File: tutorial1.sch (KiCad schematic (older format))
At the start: 5 parts, among them IC1 PIC12C508A-I/SN, J1 MYCONN3

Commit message: busses
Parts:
- added P1, P2, P3, P?: USB_OTG, symbol USB_OTG
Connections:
- net labels added: a1, a2, a3, a4, a5, a[1...5], b1, b2, b3, b4, b5
- wire segments 18 -> 38
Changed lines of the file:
@@
 $EndComp
 $Comp
-L VCC #PWR01
+L VCC #PWR1
 U 1 1 59841EA6
 P 2450 1650
-F 0 "#PWR01" H 2450 1500 50  0001 C CNN
+F 0 "#PWR1" H 2450 1500 50  0001 C CNN
 F 1 "VCC" H 2450 1800 50  0000 C CNN
 F 2 "" H 2450 1650 50  0000 C CNN
@@
 $EndComp
 $Comp
-L VCC #PWR02
+L VCC #PWR7
 U 1 1 59841EF5
 P 5150 1300
-F 0 "#PWR02" H 5150 1150 50  0001 C CNN
+F 0 "#PWR7" H 5150 1150 50  0001 C CNN
 F 1 "VCC" H 5150 1450 50  0000 C CNN
 F 2 "" H 5150 1300 50  0000 C CNN
@@
 $EndComp
 $Comp
-L VCC #PWR03
+L VCC #PWR5
 U 1 1 59841F14
 P 3550 2800
-F 0 "#PWR03" H 3550 2650 50  0001 C CNN
+F 0 "#PWR5" H 3550 2650 50  0001 C CNN
 F 1 "VCC" H 3550 2950 50  0000 C CNN
 F 2 "" H 3550 2800 50  0000 C CNN
@@
 $EndComp
 $Comp
-L GND #PWR04
+L GND #PWR2
 U 1 1 59842025
 P 2450 2550
-F 0 "#PWR04" H 2450 2300 50  0001 C CNN
+F 0 "#PWR2" H 2450 2300 50  0001 C CNN
 F 1 "GND" H 2450 2400 50  0000 C CNN
 F 2 "" H 2450 2550 50  0000 C CNN
@@
 $EndComp
 $Comp
-L GND #PWR05
+L GND #PWR6
 U 1 1 59842043
 P 3550 3200
-F 0 "#PWR05" H 3550 2950 50  0001 C CNN
+F 0 "#PWR6" H 3550 2950 50  0001 C CNN
 F 1 "GND" H 3550 3050 50  0000 C CNN
 F 2 "" H 3550 3200 50  0000 C CNN
@@
 	1    0    0    -1
 $EndComp
-Wire Wire Line
-	4050 1850 4200 1850
-Wire Wire Line
-	4200 1850 4200 1350
-Wire Wire Line
-	4050 1950 4750 1950
-Wire Wire Line
-	2650 1850 2450 1850
-Wire Wire Line
-	2450 1850 2450 1650
-Wire Wire Line
-	2650 2450 2450 2450
-Wire Wire Line
-	2450 2450 2450 2550
-Wire Wire Line
-	3400 2900 3550 2900
-Wire Wire Line
-	3550 2900 3550 2800
-Wire Wire Line
-	3400 3100 3550 3100
-Wire Wire Line
-	3550 3100 3550 3200
-Wire Wire Line
-	3400 3000 3950 3000
-Wire Wire Line
-	4250 3000 4750 3000
-Wire Wire Line
-	4600 1350 4700 1350
-Wire Wire Line
-	5000 1350 5150 1350
-Wire Wire Line
-	5150 1350 5150 1300
 Text Label 4450 1950 0    60   ~ 0
 INPUT
@@
 NoConn ~ 2500 1250
 $Comp
-L PWR_FLAG #FLG06
+L PWR_FLAG #FLG1
 U 1 1 598423A3
 P 2800 1200
-F 0 "#FLG06" H 2800 1295 50  0001 C CNN
+F 0 "#FLG1" H 2800 1295 50  0001 C CNN
 F 1 "PWR_FLAG" H 2800 1380 50  0000 C CNN
 F 2 "" H 2800 1200 50  0000 C CNN
@@
 $EndComp
 $Comp
-L PWR_FLAG #FLG07
+L PWR_FLAG #FLG2
 U 1 1 598423C1
 P 3150 1050
-F 0 "#FLG07" H 3150 1145 50  0001 C CNN
+F 0 "#FLG2" H 3150 1145 50  0001 C CNN
 F 1 "PWR_FLAG" H 3150 1230 50  0000 C CNN
 F 2 "" H 3150 1050 50  0000 C CNN
@@
 $EndComp
 $Comp
-L VCC #PWR08
+L VCC #PWR3
 U 1 1 598423E4
 P 2800 1050
-F 0 "#PWR08" H 2800 900 50  0001 C CNN
+F 0 "#PWR3" H 2800 900 50  0001 C CNN
 F 1 "VCC" H 2800 1200 50  0000 C CNN
 F 2 "" H 2800 1050 50  0000 C CNN
@@
 $EndComp
 $Comp
-L GND #PWR09
+L GND #PWR4
 U 1 1 5984246D
 P 3150 1200
-F 0 "#PWR09" H 3150 950 50  0001 C CNN
+F 0 "#PWR4" H 3150 950 50  0001 C CNN
 F 1 "GND" H 3150 1050 50  0000 C CNN
 F 2 "" H 3150 1200 50  0000 C CNN
@@
 	1    0    0    -1
 $EndComp
+$Comp
+L USB_OTG P1
+U 1 1 59AE7FC8
+P 2950 4450
+F 0 "P1" H 3275 4325 50  0000 C CNN
+F 1 "USB_OTG" H 2950 4650 50  0000 C CNN
+F 2 "" V 2900 4350 50  0000 C CNN
+F 3 "" V 2900 4350 50  0000 C CNN
+	1    2950 4450
+	0    -1   1    0
+$EndComp
+$Comp
+L USB_OTG P2
+U 1 1 59AE8338
+P 2950 5400
+F 0 "P2" H 3275 5275 50  0000 C CNN
+F 1 "USB_OTG" H 2950 5600 50  0000 C CNN
+F 2 "" V 2900 5300 50  0000 C CNN
+F 3 "" V 2900 5300 50  0000 C CNN
+	1    2950 5400
+	0    -1   1    0
+$EndComp
+$Comp
+L USB_OTG P3
+U 1 1 59AE8397
+P 2950 6350
+F 0 "P3" H 3275 6225 50  0000 C CNN
+F 1 "USB_OTG" H 2950 6550 50  0000 C CNN
+F 2 "" V 2900 6250 50  0000 C CNN
+F 3 "" V 2900 6250 50  0000 C CNN
+	1    2950 6350
+	0    -1   1    0
+$EndComp
+Text Label 3250 4250 0    60   ~ 0
+a1
+Text Label 3250 4350 0    60   ~ 0
+a2
+Text Label 3250 4450 0    60   ~ 0
+a3
+Text Label 3250 4550 0    60   ~ 0
+a4
+Text Label 3250 4650 0    60   ~ 0
+a5
+Text Label 3250 5200 0    60   ~ 0
+a1
+Text Label 3250 5300 0    60   ~ 0
+a2
+Text Label 3250 5400 0    60   ~ 0
+a3
+Text Label 3250 5500 0    60   ~ 0
+a4
+Text Label 3250 5600 0    60   ~ 0
+a5
+Text Label 3250 6150 0    60   ~ 0
+a1
+Text Label 3250 6250 0    60   ~ 0
+a2
+Text Label 3250 6350 0    60   ~ 0
+a3
+Text Label 3250 6450 0    60   ~ 0
+a4
+Text Label 3250 6550 0    60   ~ 0
+a5
+Entry Wire Line
+	3650 4250 3750 4350
+Entry Wire Line
+	3650 4350 3750 4450
+Entry Wire Line
+	3650 4450 3750 4550
+Entry Wire Line
+	3650 4550 3750 4650
+Entry Wire Line
+	3650 4650 3750 4750
+Entry Wire Line
+	3650 5200 3750 5300
+Entry Wire Line
+	3650 5300 3750 5400
+Entry Wire Line
+	3650 5400 3750 5500
+Entry Wire Line
+	3650 5500 3750 5600
+Entry Wire Line
+	3650 5600 3750 5700
+Entry Wire Line
+	3650 6150 3750 6250
+Entry Wire Line
+	3650 6250 3750 6350
+Entry Wire Line
+	3650 6350 3750 6450
+Entry Wire Line
+	3650 6450 3750 6550
+Entry Wire Line
+	3650 6550 3750 6650
+Text Label 3750 5000 0    60   ~ 0
+a[1...5]
+$Comp
+L USB_OTG P?
+U 1 1 59AF0BD4
+P 5600 4450
+F 0 "P?" H 5925 4325 50  0000 C CNN
+F 1 "USB_OTG" H 5600 4650 50  0000 C CNN
+F 2 "" V 5550 4350 50  0000 C CNN
+F 3 "" V 5550 4350 50  0000 C CNN
+	1    5600 4450
+	0    1    1    0
+$EndComp
+Text Label 5150 4250 0    60   ~ 0
+b1
+Text Label 5150 4350 0    60   ~ 0
+b2
+Text Label 5150 4450 0    60   ~ 0
+b3
+Text Label 5150 4550 0    60   ~ 0
+b4
+Text Label 5150 4650 0    60   ~ 0
+b5
+Wire Wire Line
+	4050 1850 4200 1850
+Wire Wire Line
+	4200 1850 4200 1350
+Wire Wire Line
+	4050 1950 4750 1950
+Wire Wire Line
+	2650 1850 2450 1850
+Wire Wire Line
+	2450 1850 2450 1650
+Wire Wire Line
+	2650 2450 2450 2450
+Wire Wire Line
+	2450 2450 2450 2550
+Wire Wire Line
+	3400 2900 3550 2900
+Wire Wire Line
+	3550 2900 3550 2800
+Wire Wire Line
+	3400 3100 3550 3100
+Wire Wire Line
+	3550 3100 3550 3200
+Wire Wire Line
+	3400 3000 3950 3000
+Wire Wire Line
+	4250 3000 4750 3000
+Wire Wire Line
+	4600 1350 4700 1350
+Wire Wire Line
+	5000 1350 5150 1350
+Wire Wire Line
+	5150 1350 5150 1300
 Wire Wire Line
 	3150 1050 3150 1200
 Wire Wire Line
 	2800 1200 2800 1050
+Wire Bus Line
+	3750 4200 3750 6700
+Wire Wire Line
+	3250 4250 3650 4250
+Wire Wire Line
+	3250 4350 3650 4350
+Wire Wire Line
+	3250 4450 3650 4450
+Wire Wire Line
+	3250 4550 3650 4550
+Wire Wire Line
+	3250 4650 3650 4650
+Wire Wire Line
+	3250 5200 3650 5200
+Wire Wire Line
+	3250 5300 3650 5300
+Wire Wire Line
+	3250 5400 3650 5400
+Wire Wire Line
+	3250 5500 3650 5500
+Wire Wire Line
+	3250 5600 3650 5600
+Wire Wire Line
+	3250 6150 3650 6150
+Wire Wire Line
+	3250 6250 3650 6250
+Wire Wire Line
+	3250 6350 3650 6350
+Wire Wire Line
+	3250 6450 3650 6450
+Wire Wire Line
+	3250 6550 3650 6550
+Wire Bus Line
+	4850 4050 4850 5150
+Wire Wire Line
+	5300 4250 4950 4250
+Wire Wire Line
+	5300 4350 4950 4350
+Wire Wire Line
+	5300 4450 4950 4450
+Wire Wire Line
+	5300 4550 4950 4550
+Wire Wire Line
+	5300 4650 4950 4650
+Entry Wire Line
+	4850 4550 4950 4650
+Entry Wire Line
+	4850 4450 4950 4550
+Entry Wire Line
+	4850 4350 4950 4450
+Entry Wire Line
+	4850 4250 4950 4350
+Entry Wire Line
+	4850 4150 4950 4250
 $EndSCHEMATC

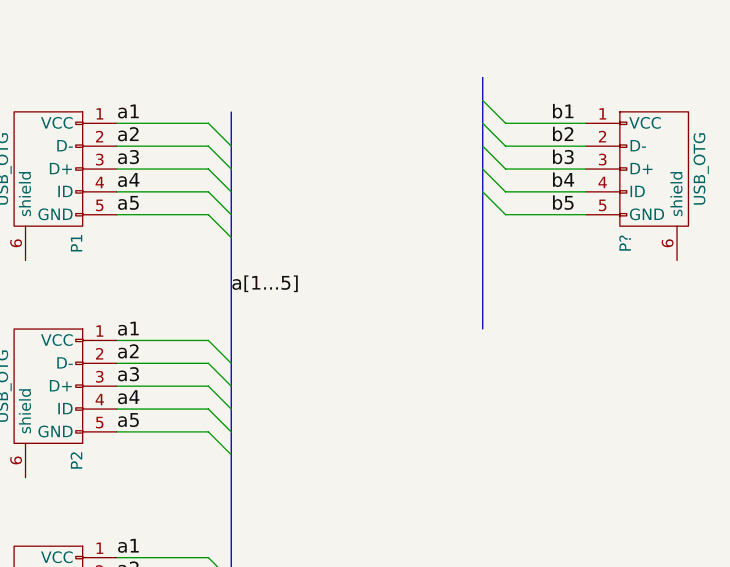
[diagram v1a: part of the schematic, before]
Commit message: bus labels
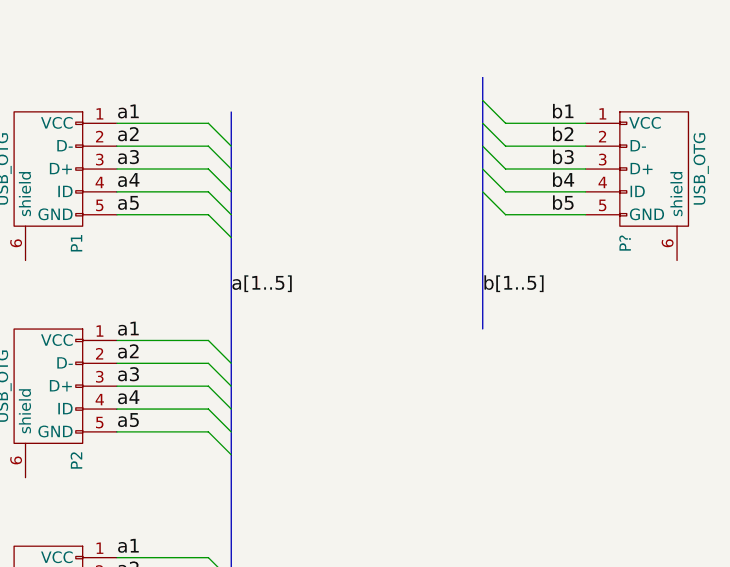
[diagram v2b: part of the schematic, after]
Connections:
- net labels added: a[1..5], b[1..5]
- net labels removed: a[1...5]
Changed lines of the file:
@@
 	3650 6550 3750 6650
 Text Label 3750 5000 0    60   ~ 0
-a[1...5]
+a[1..5]
 $Comp
 L USB_OTG P?
@@
 Entry Wire Line
 	4850 4150 4950 4250
+Text Label 4850 5000 0    60   ~ 0
+b[1..5]
 $EndSCHEMATC
